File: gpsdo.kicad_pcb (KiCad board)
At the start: 2 copper layers, 175 parts, among them J1 OLED, J10 10MHZ_OUT, J11 100MHZ_OUT, J12 10MHZ_OUT, J13 10MHZ_OUT, J14 10MHZ_OUT, J15 10MHZ_OUT, J2 ARDUINO_UART, J3 VOLTMETER, J4 ARDUINO_EXTRA_PINS, J5 POWER_IN, J6 GPS_ANT, J7 10MHZ_OUT, J8 10MHZ_OUT, J9 10MHZ_OUT, U1 TPS79301-EP, U10 MSA-0385, U11 MSA-0385, U12 MSA-0385, U13 MSA-0385, U14 MSA-0385, U15 MSA-0385, U16 MSA-0385, U17 MSA-0385, U18 MSA-0385, U19 MSA-0385, U2 TPS79301-EP, U20 MSA-0385, U3 LM317DCYR, U4 SN74HC244, U5 DAC8571IDGKR, U6 LEA-M8F, U7 CVSS-945, U8 SN74HC244, U9 MC12080

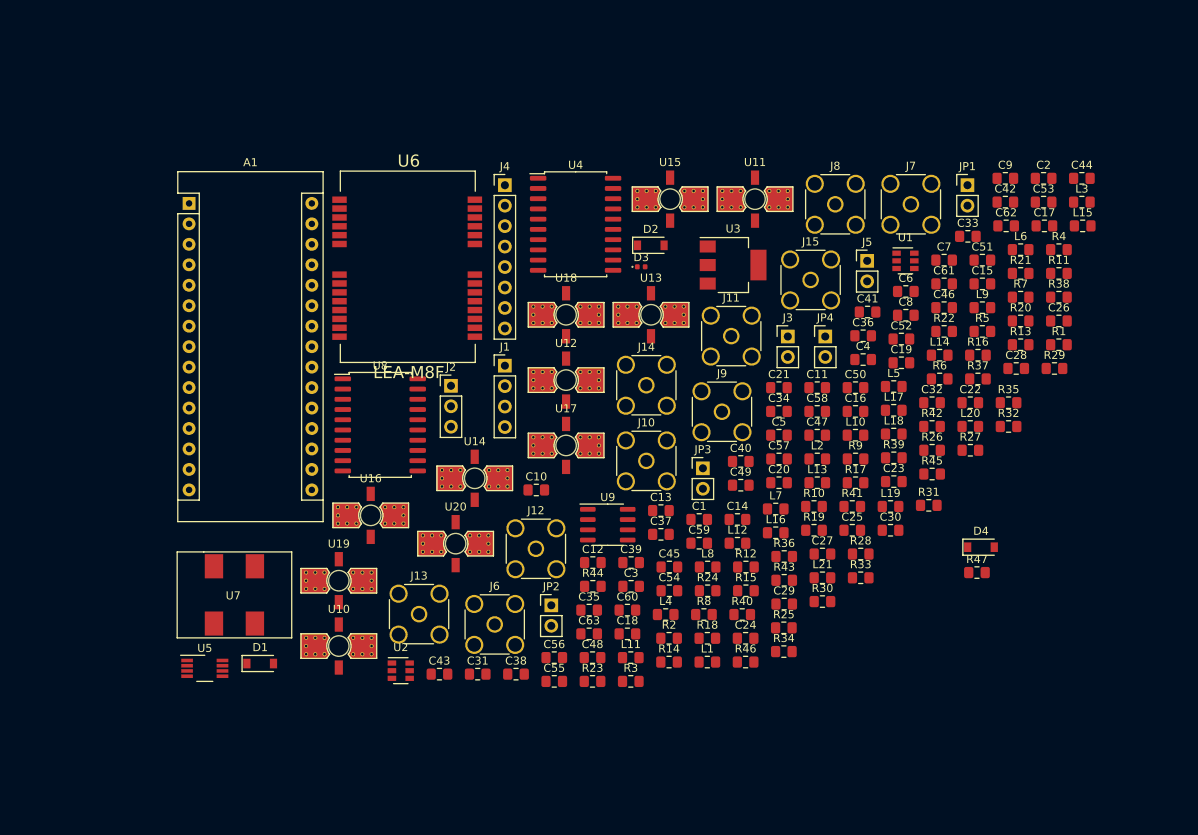
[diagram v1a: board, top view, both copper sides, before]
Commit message: Made ERC pass and updated footprint assignments
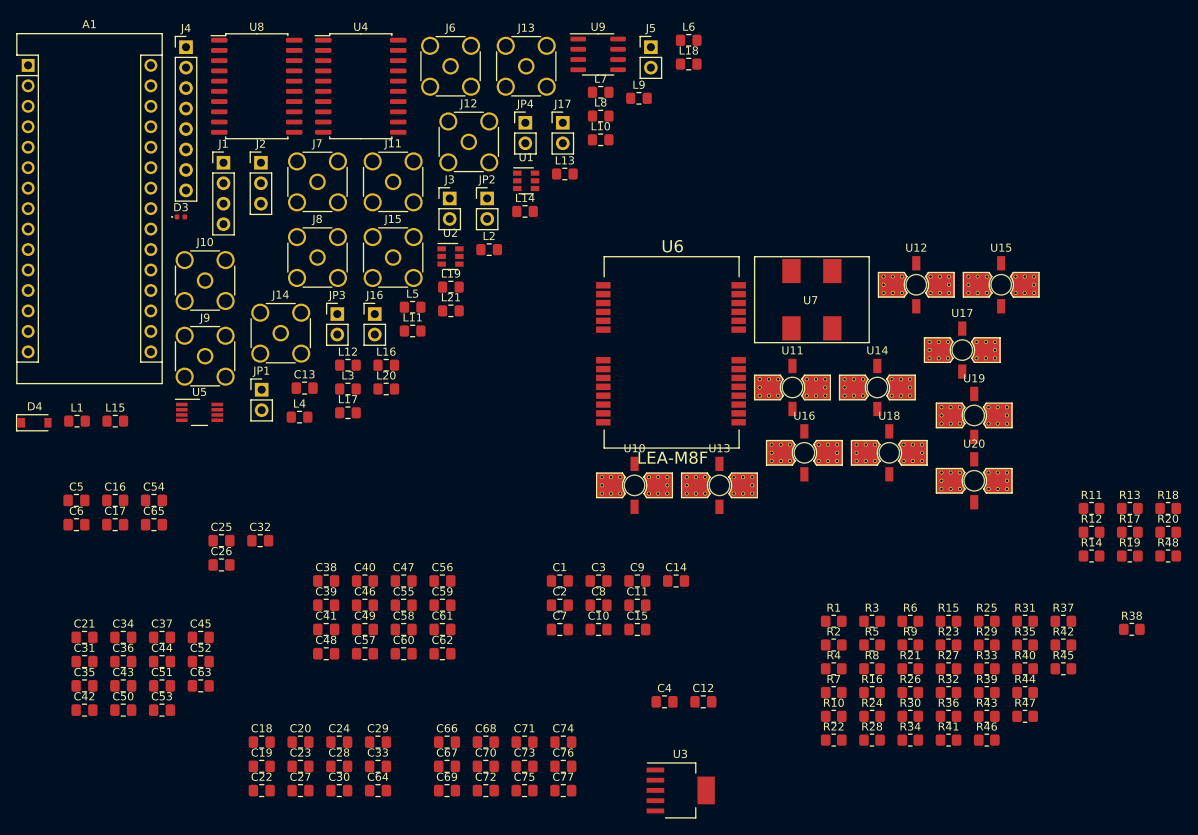
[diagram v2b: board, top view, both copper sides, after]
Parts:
- removed D1, D2: 1N4148W, Diode_SMD:D_SOD-123
- added C64: 1nF, Capacitor_SMD:C_0805_2012Metric_Pad1.18x1.45mm_HandSolder, F.Cu at (101.4, 129.0)
- added C65: 0.1uF, Capacitor_SMD:C_0805_2012Metric_Pad1.18x1.45mm_HandSolder, F.Cu at (73.6, 96.0)
- added C66: 0.1uF, Capacitor_SMD:C_0805_2012Metric_Pad1.18x1.45mm_HandSolder, F.Cu at (110.0, 123.0)
- added C67: 0.1uF, Capacitor_SMD:C_0805_2012Metric_Pad1.18x1.45mm_HandSolder, F.Cu at (110.0, 126.0)
- added C68: 0.1uF, Capacitor_SMD:C_0805_2012Metric_Pad1.18x1.45mm_HandSolder, F.Cu at (114.8, 123.0)
- added C69: 0.1uF, Capacitor_SMD:C_0805_2012Metric_Pad1.18x1.45mm_HandSolder, F.Cu at (110.0, 129.0)
- added C70: 0.1uF, Capacitor_SMD:C_0805_2012Metric_Pad1.18x1.45mm_HandSolder, F.Cu at (114.8, 126.0)
- added C71: 0.1uF, Capacitor_SMD:C_0805_2012Metric_Pad1.18x1.45mm_HandSolder, F.Cu at (119.6, 123.0)
- added C72: 0.1uF, Capacitor_SMD:C_0805_2012Metric_Pad1.18x1.45mm_HandSolder, F.Cu at (114.8, 129.0)
- added C73: 0.1uF, Capacitor_SMD:C_0805_2012Metric_Pad1.18x1.45mm_HandSolder, F.Cu at (119.6, 126.0)
- added C74: 0.1uF, Capacitor_SMD:C_0805_2012Metric_Pad1.18x1.45mm_HandSolder, F.Cu at (124.4, 123.0)
- added C75: 0.1uF, Capacitor_SMD:C_0805_2012Metric_Pad1.18x1.45mm_HandSolder, F.Cu at (119.6, 129.0)
- added C76: 0.1uF, Capacitor_SMD:C_0805_2012Metric_Pad1.18x1.45mm_HandSolder, F.Cu at (124.4, 126.0)
- added C77: 0.1uF, Capacitor_SMD:C_0805_2012Metric_Pad1.18x1.45mm_HandSolder, F.Cu at (124.4, 129.0)
- added J16: LED, Connector_PinHeader_2.54mm:PinHeader_1x02_P2.54mm_Vertical, F.Cu at (101.0, 69.9)
- added J17: TIMEPULSE, Connector_PinHeader_2.54mm:PinHeader_1x02_P2.54mm_Vertical, F.Cu at (124.4, 46.1)
- added R48: 50Ω, Resistor_SMD:R_0805_2012Metric_Pad1.20x1.40mm_HandSolder, F.Cu at (199.5, 99.9)
- C1, C10, C11, C14, C15, C16, C17, C18, C19, C2, C20, C21, C22, C23, C24, C25, C26, C27, C28, C29, C3, C30, C31, C32, C33, C34, C35, C36, C37, C38, C39, C40, C41, C42, C43, C44, C45, C46, C47, C48, C49, C5, C50, C51, C52, C53, C54, C55, C56, C57, C58, C59, C6, C60, C61, C62, C63, C7, C8, C9: footprint Capacitor_SMD:C_0805_2012Metric_Pad1.15x1.40mm_HandSolder -> Capacitor_SMD:C_0805_2012Metric_Pad1.18x1.45mm_HandSolder
- C12, C4: value 1uF -> 10uF/16V,ESR<3; footprint Capacitor_SMD:C_0805_2012Metric_Pad1.15x1.40mm_HandSolder -> Capacitor_SMD:C_0805_2012Metric_Pad1.18x1.45mm_HandSolder
- C13: value 1uF -> 47uF/10V; footprint Capacitor_SMD:C_0805_2012Metric_Pad1.15x1.40mm_HandSolder -> Capacitor_SMD:C_0805_2012Metric_Pad1.18x1.45mm_HandSolder
- R1, R10, R11, R12, R13, R14, R15, R16, R17, R18, R19, R2, R20, R21, R22, R23, R24, R25, R26, R27, R28, R29, R3, R30, R31, R32, R33, R34, R35, R36, R37, R38, R39, R4, R40, R41, R42, R43, R44, R45, R46, R47, R7, R8, R9: footprint Resistor_SMD:R_0805_2012Metric_Pad1.15x1.40mm_HandSolder -> Resistor_SMD:R_0805_2012Metric_Pad1.20x1.40mm_HandSolder
- R5: value 1.3KΩ -> 16KΩ; footprint Resistor_SMD:R_0805_2012Metric_Pad1.15x1.40mm_HandSolder -> Resistor_SMD:R_0805_2012Metric_Pad1.20x1.40mm_HandSolder
- R6: value 240Ω -> 4KΩ; footprint Resistor_SMD:R_0805_2012Metric_Pad1.15x1.40mm_HandSolder -> Resistor_SMD:R_0805_2012Metric_Pad1.20x1.40mm_HandSolder
- U3: value LM317DCYR -> TPS7A4501DCQT; footprint Package_TO_SOT_SMD:SOT-223 -> Package_TO_SOT_SMD:SOT-223-6
- moved C42 130.5 mm to (65.0, 119.0)
- moved C44 129.0 mm to (74.6, 113.0)
- moved C53 126.3 mm to (74.6, 119.0)
- moved L15 122.5 mm to (68.8, 83.2)
- moved C17 121.2 mm to (68.8, 96.0)
- moved D4 118.5 mm to (58.8, 83.4)
- moved C51 114.7 mm to (74.6, 116.0)
- moved C26 108.3 mm to (82.0, 101.0)
- moved C6 106.9 mm to (64.0, 96.0)
- moved C36 100.3 mm to (69.8, 113.0)
- moved C22 100.3 mm to (87.0, 129.0)
- moved C50 99.3 mm to (69.8, 119.0)
- moved C33 98.4 mm to (101.4, 126.0)
- moved C28 97.5 mm to (96.6, 126.0)
- moved C52 95.7 mm to (79.4, 113.0)
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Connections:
- A1 pad 11: (no net) -> ARDUINO_D8
- A1 pad 16: (no net) -> LED
- C10 pad 1: V_VCXO -> Net-(C10-Pad1)
- C10 pad 2: Net-(C10-Pad2) -> V_VCXO
- C12 pad 1: GND -> V_MMIC
- C12 pad 2: Net-(C12-Pad2) -> GND
- C13 pad 1: GND -> Net-(C13-Pad1)
- C13 pad 2: V_MMIC -> GND
- C23 pad 2: Net-(C23-Pad2) -> Net-(C13-Pad1)
- C4 pad 1: GND -> V_IN
- C4 pad 2: V_IN -> GND
- C9 pad 1: V_GPS -> Net-(C9-Pad1)
- C9 pad 2: Net-(C9-Pad2) -> V_GPS
- D4 pad 1: GND -> Net-(D4-Pad1)
- J4 pad 7: ARDUINO_D7 -> ARDUINO_D8
- L3 pad 2: Net-(C23-Pad2) -> Net-(C13-Pad1)
- R10 pad 1: V_VCXO -> Net-(C10-Pad1)
- R16 pad 2: (no net) -> Net-(C21-Pad2)
- R19 pad 1: Net-(C27-Pad1) -> Net-(C64-Pad1)
- R31 pad 1: V_MMIC -> V_MMIC2
- R39 pad 1: V_MMIC -> V_MMIC2
- R40 pad 1: V_MMIC -> V_MMIC2
- R41 pad 1: V_MMIC -> V_MMIC2
- R42 pad 1: V_MMIC -> V_MMIC2
- R5 pad 1: Net-(C12-Pad2) -> V_MMIC
- R5 pad 2: GND -> Net-(R5-Pad2)
- R6 pad 1: V_MMIC -> Net-(R5-Pad2)
- R6 pad 2: Net-(C12-Pad2) -> GND
- R7 pad 1: Net-(C9-Pad2) -> V_GPS
- R7 pad 2: V_GPS -> Net-(C9-Pad1)
- R8 pad 1: Net-(C10-Pad2) -> V_VCXO
- R8 pad 2: V_VCXO -> Net-(C10-Pad1)
- R9 pad 1: V_GPS -> Net-(C9-Pad1)
- U1 pad 5: V_GPS -> Net-(C9-Pad1)
- U1 pad 6: Net-(C9-Pad2) -> V_GPS
- U15 pad 2: GND -> V_MMIC
- U15 pad 4: GND -> V_MMIC
- U17 pad 2: GND -> V_MMIC
- U17 pad 4: GND -> V_MMIC
- U18 pad 2: GND -> V_MMIC
- U18 pad 4: GND -> V_MMIC
- U19 pad 2: GND -> V_MMIC
- U19 pad 4: GND -> V_MMIC
- U2 pad 5: V_VCXO -> Net-(C10-Pad1)
- U2 pad 6: Net-(C10-Pad2) -> V_VCXO
- U20 pad 2: GND -> V_MMIC
- U20 pad 4: GND -> V_MMIC
- U3 pad 1: Net-(C12-Pad2) -> V_IN
- U3 pad 2: V_MMIC -> V_IN
- U3 pad 3: V_IN -> GND
- U4 pad 14: (no net) -> TIMEPULSE
- U4 pad 16: A2G_RX -> Net-(D4-Pad1)
- U7 pad 4: Net-(C23-Pad2) -> Net-(C13-Pad1)
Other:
- rule pad_to_mask_clearance: 0.051 -> 0

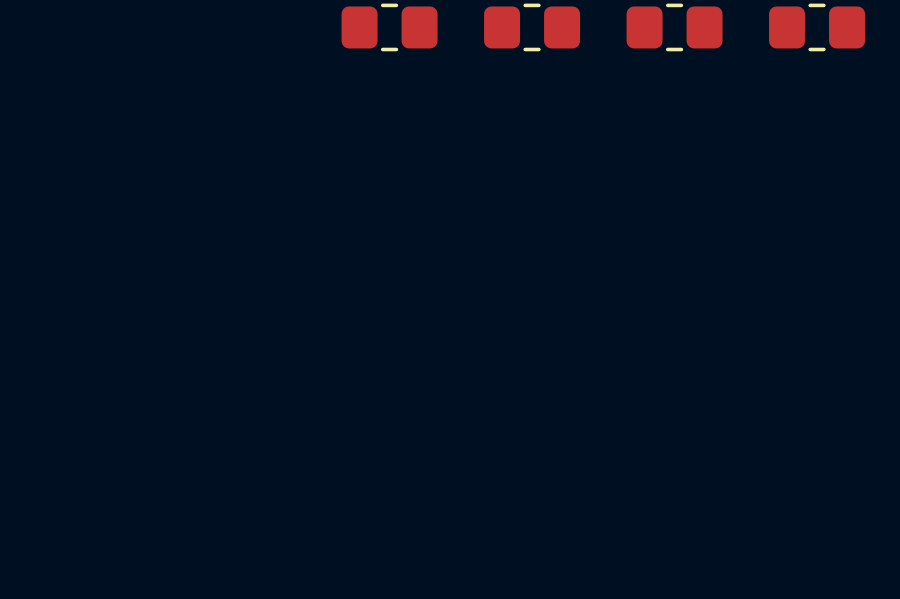
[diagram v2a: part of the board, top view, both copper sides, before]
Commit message: Reworked V_MMIC resistors for 5.5V and added V_MMIC2 for 11.13V
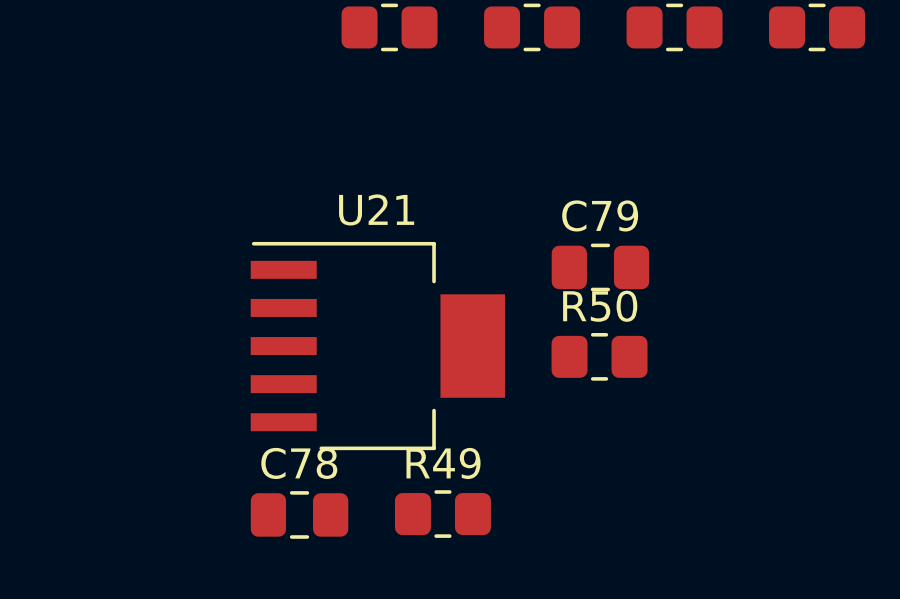
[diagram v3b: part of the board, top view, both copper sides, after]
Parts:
- added C78: 10uF/16V,ESR<3, Capacitor_SMD:C_0805_2012Metric_Pad1.18x1.45mm_HandSolder, F.Cu at (155.0, 139.0)
- added C79: 10uF/16V,ESR<3, Capacitor_SMD:C_0805_2012Metric_Pad1.18x1.45mm_HandSolder, F.Cu at (165.0, 130.8)
- added R49: 14.7KΩ, Resistor_SMD:R_0805_2012Metric_Pad1.20x1.40mm_HandSolder, F.Cu at (159.8, 139.0)
- added R50: 1.8KΩ, Resistor_SMD:R_0805_2012Metric_Pad1.20x1.40mm_HandSolder, F.Cu at (165.0, 133.7)
- added U21: TPS7A4501DCQT, Package_TO_SOT_SMD:SOT-223-6, F.Cu at (157.6, 133.4)
- R5: value 16KΩ -> 15KΩ
- R6: value 4KΩ -> 4.3KΩ

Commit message: checked
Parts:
- C18: value 0.1uF -> 22uF
- C19, C20: value 1uF -> 22uF
- R11: value TBD -> 1k0
- R12: value TBD -> NF
- R13: value 10K -> 100K
- R14: value 10K -> 1000K
- R17: value 16.7Ω -> 15Ω
- R18, R19: value 16.7Ω 1% -> 15Ω
- R26, R27, R28, R29, R30, R31, R38, R39, R40, R41, R42: value 86.6Ω 1% -> 22Ω
- R48: value 50Ω -> 47Ω
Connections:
- A1 pad 15: (no net) -> Net-(A1-Pad15)
- A1 pad 17: (no net) -> Net-(A1-Pad17)
- A1 pad 18: (no net) -> Net-(A1-Pad18)
- A1 pad 19: (no net) -> Net-(A1-Pad19)
- A1 pad 20: (no net) -> Net-(A1-Pad20)
- A1 pad 21: (no net) -> Net-(A1-Pad21)
- A1 pad 22: (no net) -> Net-(A1-Pad22)
- A1 pad 25: (no net) -> Net-(A1-Pad25)
- A1 pad 26: (no net) -> Net-(A1-Pad26)
- A1 pad 28: (no net) -> Net-(A1-Pad28)
- A1 pad 3: (no net) -> Net-(A1-Pad3)
- U4 pad 11: (no net) -> Net-(U4-Pad11)
- U4 pad 13: (no net) -> Net-(U4-Pad13)
- U4 pad 15: (no net) -> Net-(U4-Pad15)
- U4 pad 17: (no net) -> Net-(U4-Pad17)
- U4 pad 3: (no net) -> Net-(U4-Pad3)
- U4 pad 5: (no net) -> Net-(U4-Pad5)
- U4 pad 7: (no net) -> Net-(U4-Pad7)
- U4 pad 9: (no net) -> Net-(U4-Pad9)
- U6 pad 1: (no net) -> Net-(U6-Pad1)
- U6 pad 10: (no net) -> Net-(U6-Pad10)
- U6 pad 12: (no net) -> Net-(U6-Pad12)
- U6 pad 2: (no net) -> Net-(U6-Pad2)
- U6 pad 20: (no net) -> Net-(U6-Pad20)
- U6 pad 24: (no net) -> Net-(U6-Pad24)
- U6 pad 25: (no net) -> Net-(U6-Pad25)
- U6 pad 26: (no net) -> Net-(U6-Pad26)
- U6 pad 27: (no net) -> Net-(U6-Pad27)
- U6 pad 5: (no net) -> Net-(U6-Pad5)
- U6 pad 8: (no net) -> Net-(U6-Pad8)
- U6 pad 9: (no net) -> Net-(U6-Pad9)
- U8 pad 11: (no net) -> Net-(U8-Pad11)
- U8 pad 12: (no net) -> Net-(C32-Pad1)
- U8 pad 13: (no net) -> Net-(U8-Pad13)
- U8 pad 14: Net-(JP4-Pad2) -> Net-(C32-Pad1)
- U8 pad 15: (no net) -> Net-(U8-Pad15)
- U8 pad 16: Net-(JP3-Pad2) -> Net-(C32-Pad1)
- U8 pad 17: (no net) -> Net-(U8-Pad17)
- U8 pad 3: (no net) -> Net-(U8-Pad3)
- U8 pad 4: Net-(JP1-Pad1) -> Net-(C21-Pad2)
- U8 pad 5: (no net) -> Net-(U8-Pad5)
- U8 pad 6: Net-(JP2-Pad1) -> Net-(C21-Pad2)
- U8 pad 7: (no net) -> Net-(U8-Pad7)
- U8 pad 8: (no net) -> Net-(C21-Pad2)
- U8 pad 9: (no net) -> Net-(U8-Pad9)

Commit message: Changed U8 buffer to 74HC541
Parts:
- removed JP1: JP_BUF_1_IN, Connector_PinHeader_2.54mm:PinHeader_1x02_P2.54mm_Vertical
- removed JP2: JP_BUF_2_IN, Connector_PinHeader_2.54mm:PinHeader_1x02_P2.54mm_Vertical
- removed JP3: JP_BUF_1_OUT, Connector_PinHeader_2.54mm:PinHeader_1x02_P2.54mm_Vertical
- removed JP4: JP_BUF_2_OUT, Connector_PinHeader_2.54mm:PinHeader_1x02_P2.54mm_Vertical
- U8: value SN74HC244 -> SN74HC541DWR
- moved U8 71.9 mm to (49.0, 103.0)
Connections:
- A1 pad 15: Net-(A1-Pad15) -> (no net)
- A1 pad 17: Net-(A1-Pad17) -> (no net)
- A1 pad 18: Net-(A1-Pad18) -> (no net)
- A1 pad 19: Net-(A1-Pad19) -> (no net)
- A1 pad 20: Net-(A1-Pad20) -> (no net)
- A1 pad 21: Net-(A1-Pad21) -> (no net)
- A1 pad 22: Net-(A1-Pad22) -> (no net)
- A1 pad 25: Net-(A1-Pad25) -> (no net)
- A1 pad 26: Net-(A1-Pad26) -> (no net)
- A1 pad 28: Net-(A1-Pad28) -> (no net)
- A1 pad 3: Net-(A1-Pad3) -> (no net)
- U4 pad 11: Net-(U4-Pad11) -> (no net)
- U4 pad 13: Net-(U4-Pad13) -> (no net)
- U4 pad 15: Net-(U4-Pad15) -> (no net)
- U4 pad 17: Net-(U4-Pad17) -> (no net)
- U4 pad 3: Net-(U4-Pad3) -> (no net)
- U4 pad 5: Net-(U4-Pad5) -> (no net)
- U4 pad 7: Net-(U4-Pad7) -> (no net)
- U4 pad 9: Net-(U4-Pad9) -> (no net)
- U6 pad 1: Net-(U6-Pad1) -> (no net)
- U6 pad 10: Net-(U6-Pad10) -> (no net)
- U6 pad 12: Net-(U6-Pad12) -> (no net)
- U6 pad 2: Net-(U6-Pad2) -> (no net)
- U6 pad 20: Net-(U6-Pad20) -> (no net)
- U6 pad 24: Net-(U6-Pad24) -> (no net)
- U6 pad 25: Net-(U6-Pad25) -> (no net)
- U6 pad 26: Net-(U6-Pad26) -> (no net)
- U6 pad 27: Net-(U6-Pad27) -> (no net)
- U6 pad 5: Net-(U6-Pad5) -> (no net)
- U6 pad 8: Net-(U6-Pad8) -> (no net)
- U6 pad 9: Net-(U6-Pad9) -> (no net)
- U8 pad 11: Net-(U8-Pad11) -> (no net)
- U8 pad 12: Net-(C32-Pad1) -> (no net)
- U8 pad 13: Net-(U8-Pad13) -> (no net)
- U8 pad 14: Net-(C32-Pad1) -> (no net)
- U8 pad 15: Net-(U8-Pad15) -> Net-(C32-Pad1)
- U8 pad 17: Net-(U8-Pad17) -> Net-(C32-Pad1)
- U8 pad 3: Net-(U8-Pad3) -> Net-(C21-Pad2)
- U8 pad 5: Net-(U8-Pad5) -> Net-(C21-Pad2)
- U8 pad 6: Net-(C21-Pad2) -> (no net)
- U8 pad 7: Net-(U8-Pad7) -> (no net)
- U8 pad 8: Net-(C21-Pad2) -> (no net)
- U8 pad 9: Net-(U8-Pad9) -> (no net)

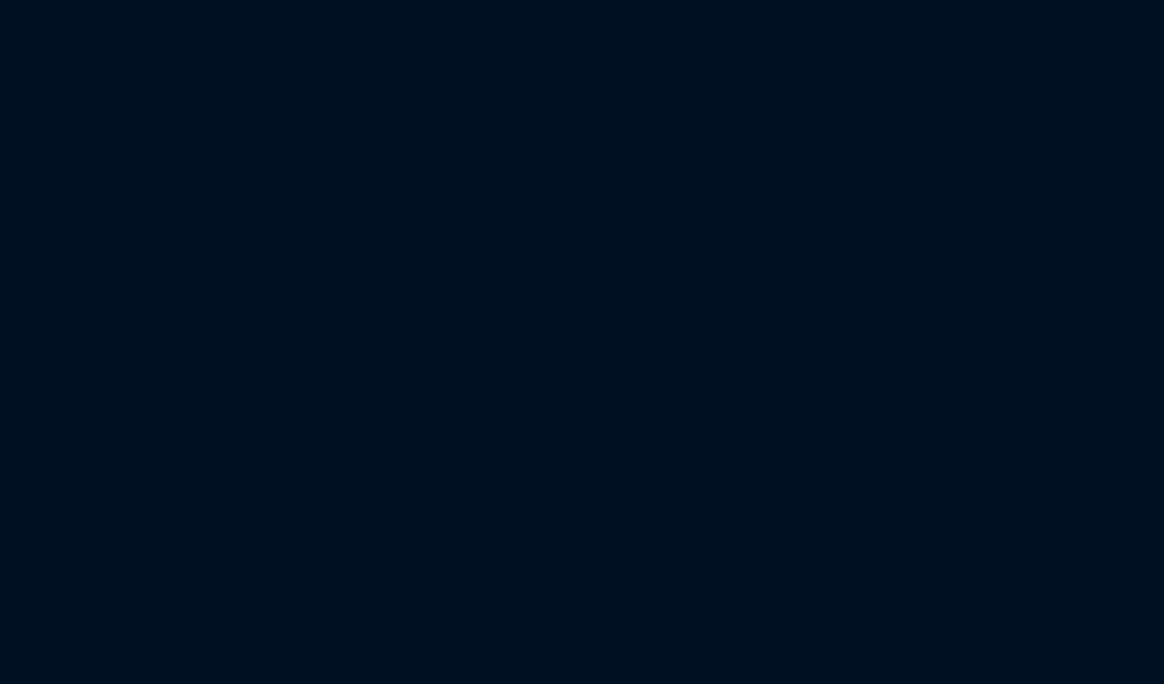
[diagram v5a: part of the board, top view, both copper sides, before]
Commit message: Added GPS pins and mounting holes
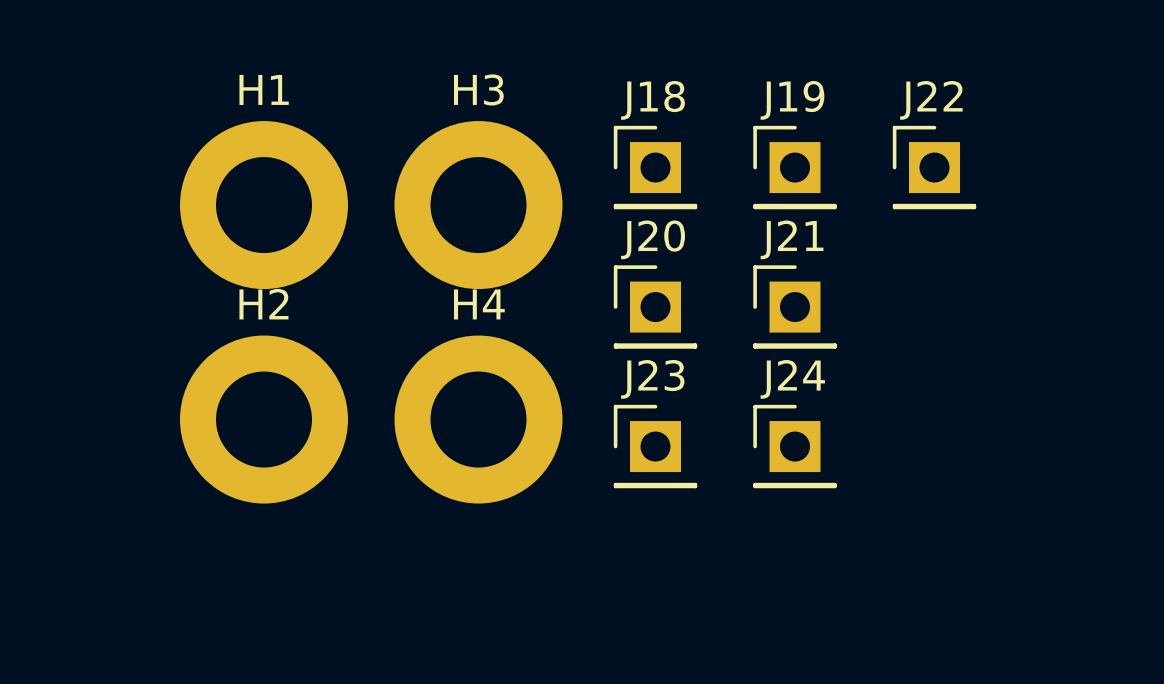
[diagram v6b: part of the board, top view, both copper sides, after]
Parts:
- added H1: MountingHole_Pad, MountingHole:MountingHole_3.2mm_M3_DIN965_Pad, F.Cu at (162.0, 36.0)
- added H2: MountingHole_Pad, MountingHole:MountingHole_3.2mm_M3_DIN965_Pad, F.Cu at (162.0, 43.1)
- added H3: MountingHole_Pad, MountingHole:MountingHole_3.2mm_M3_DIN965_Pad, F.Cu at (169.2, 36.0)
- added H4: MountingHole_Pad, MountingHole:MountingHole_3.2mm_M3_DIN965_Pad, F.Cu at (169.2, 43.1)
- added J18: TAP_GPS_TX, Connector_PinHeader_2.54mm:PinHeader_1x01_P2.54mm_Vertical, F.Cu at (175.1, 34.8)
- added J19: TAP_GPS_RX, Connector_PinHeader_2.54mm:PinHeader_1x01_P2.54mm_Vertical, F.Cu at (179.7, 34.8)
- added J20: TAP_DAC_SDA, Connector_PinHeader_2.54mm:PinHeader_1x01_P2.54mm_Vertical, F.Cu at (175.1, 39.4)
- added J21: TAP_DAC_SCL, Connector_PinHeader_2.54mm:PinHeader_1x01_P2.54mm_Vertical, F.Cu at (179.7, 39.4)
- added J22: TAP_GPS_RF_IN, Connector_PinHeader_2.54mm:PinHeader_1x01_P2.54mm_Vertical, F.Cu at (184.3, 34.8)
- added J23: TAP_GPS_TPLS, Connector_PinHeader_2.54mm:PinHeader_1x01_P2.54mm_Vertical, F.Cu at (175.1, 44.0)
- added J24: TAP_GPS_V_ANT, Connector_PinHeader_2.54mm:PinHeader_1x01_P2.54mm_Vertical, F.Cu at (179.7, 44.0)
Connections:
- net Net-(U6-Pad18) renamed GPS_V_ANT
